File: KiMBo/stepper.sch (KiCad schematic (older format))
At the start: 22 parts

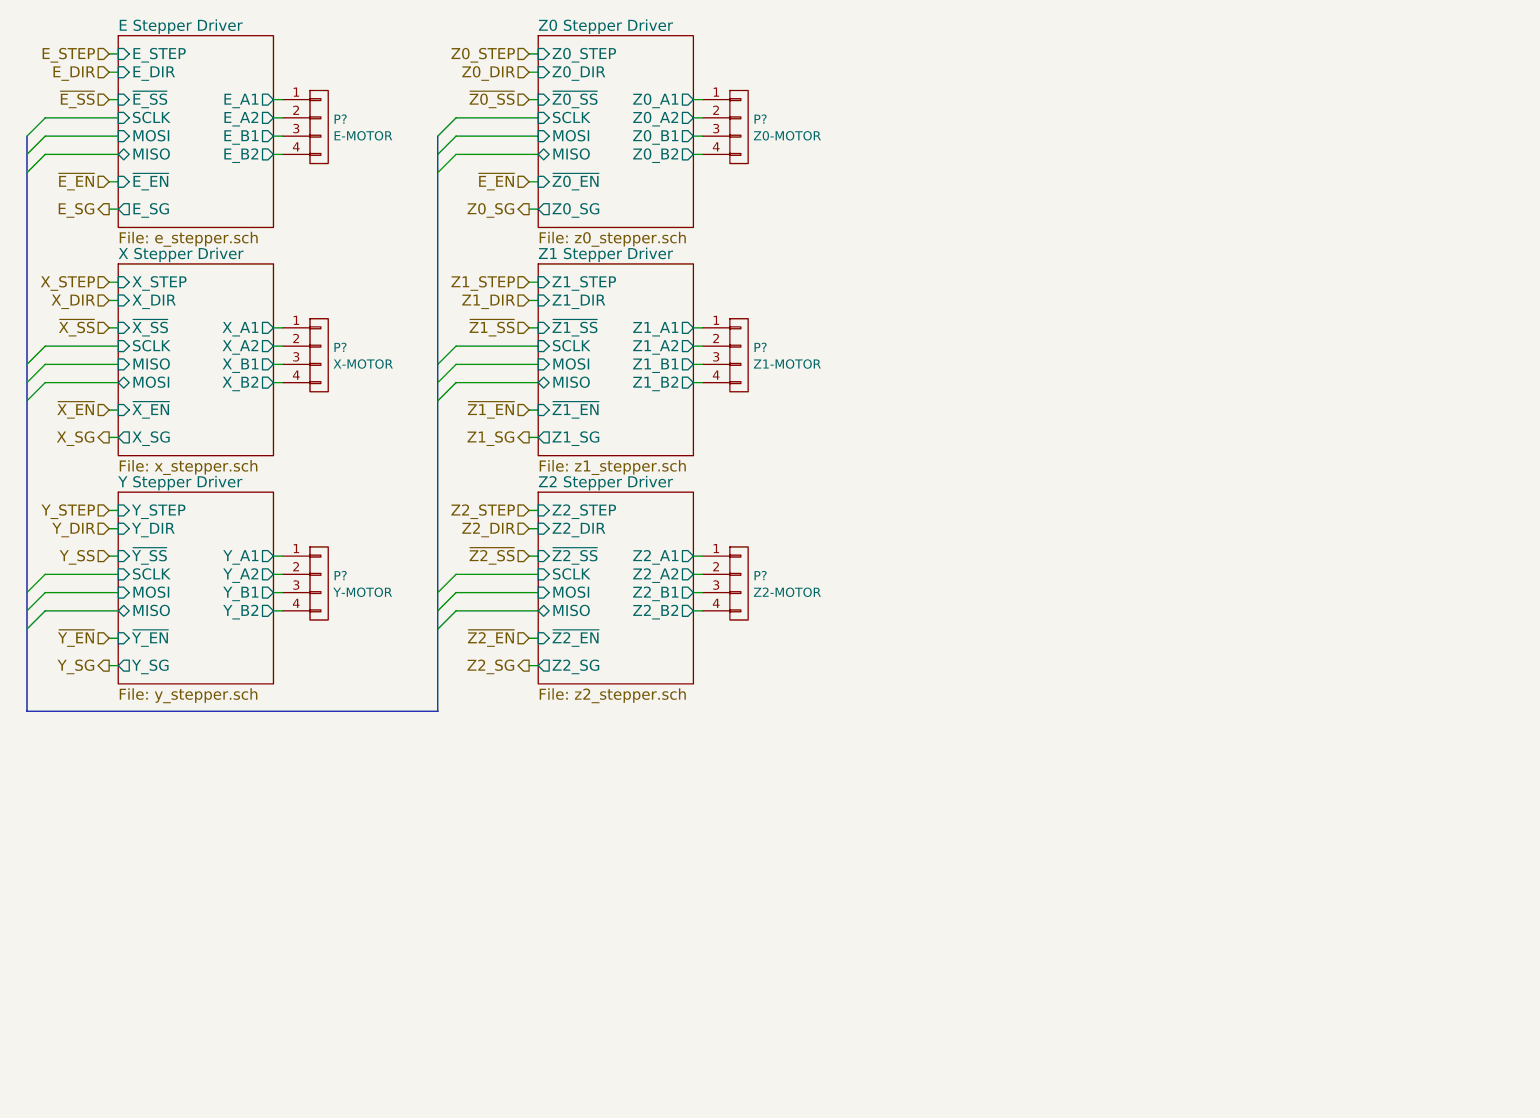
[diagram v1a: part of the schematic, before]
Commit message: Use the TMC2130 stepper driver, document and calculate the stepper motor current
The current to the motors are set by IRUN and IHOLD of the IHOLD_IRUN register
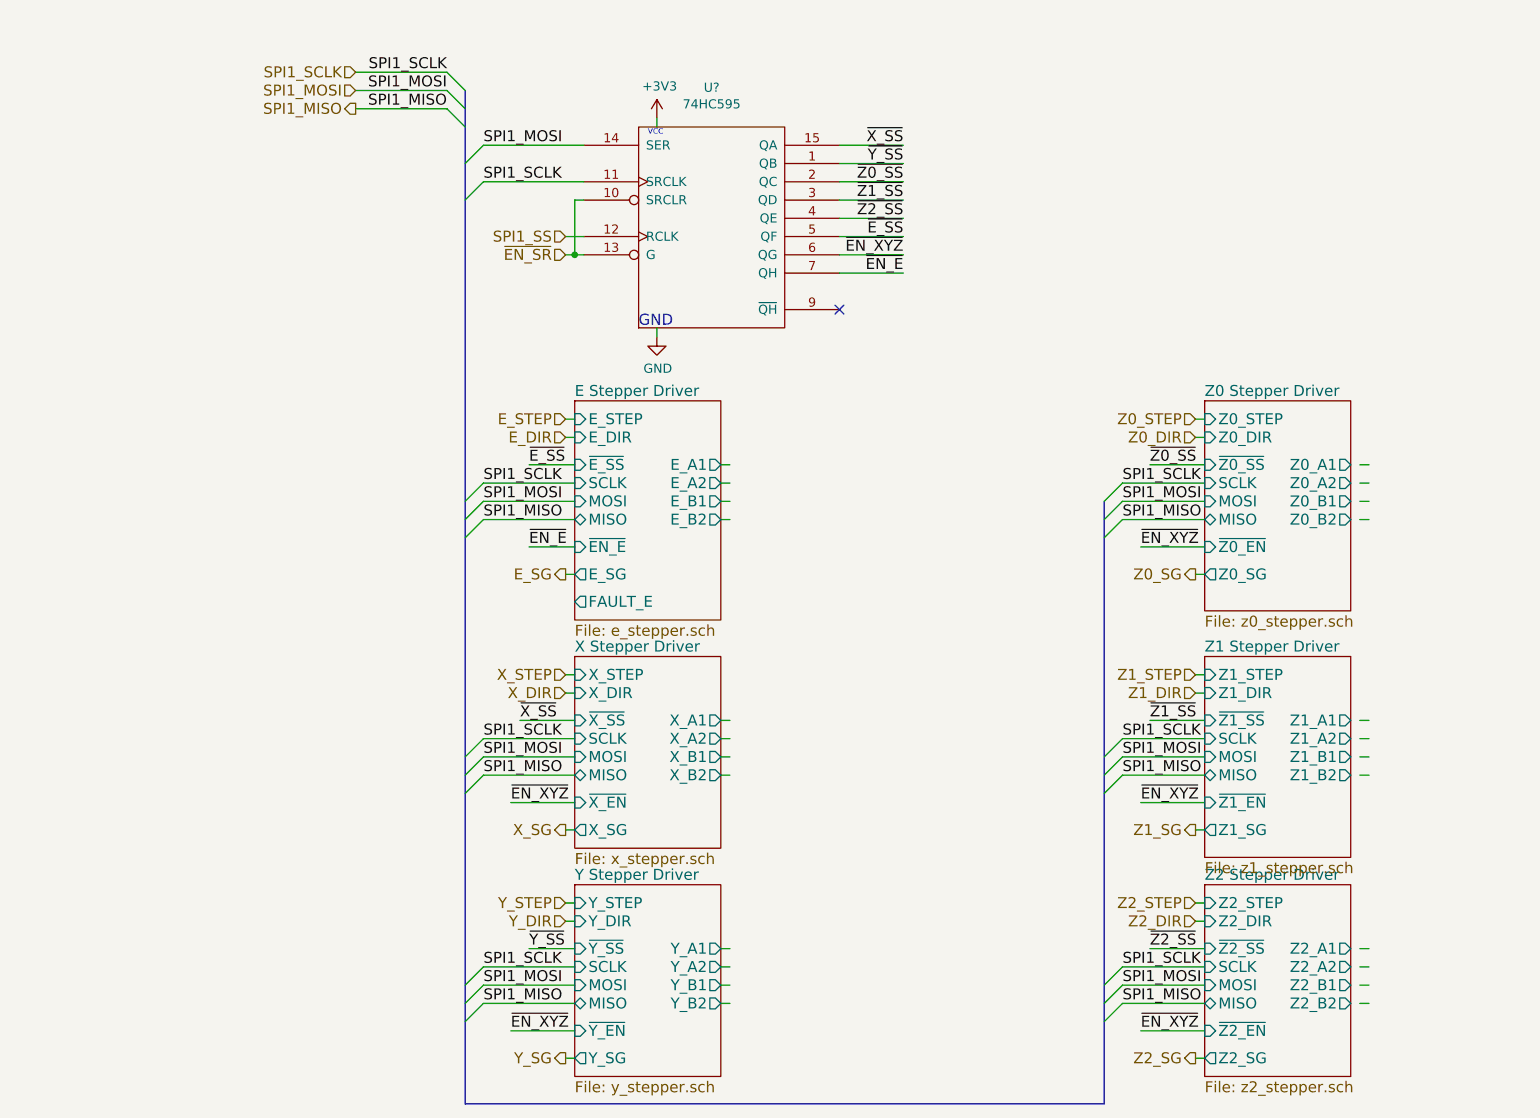
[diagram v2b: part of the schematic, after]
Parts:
- removed P?: E-MOTOR, symbol CONN_01X04
- removed P?: X-MOTOR, symbol CONN_01X04
- removed P?: Y-MOTOR, symbol CONN_01X04
- removed P?: Z0-MOTOR, symbol CONN_01X04
- removed P?: Z1-MOTOR, symbol CONN_01X04
- removed P?: Z2-MOTOR, symbol CONN_01X04
- added U?: 74HC595, symbol 74HC595
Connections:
- net labels added: +3V3, SPI1_MISO, SPI1_MOSI, SPI1_SCLK, SPI1_SS, ~EN_E, ~EN_SR, ~EN_XYZ, ~Y_SS
- net labels removed: Y_SS, ~E_EN, ~X_EN, ~Y_EN, ~Z1_EN, ~Z2_EN
- wire segments 124 -> 143
- no-connect marks 0 -> 1
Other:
- note added: "GND"
- note added: "VCC"

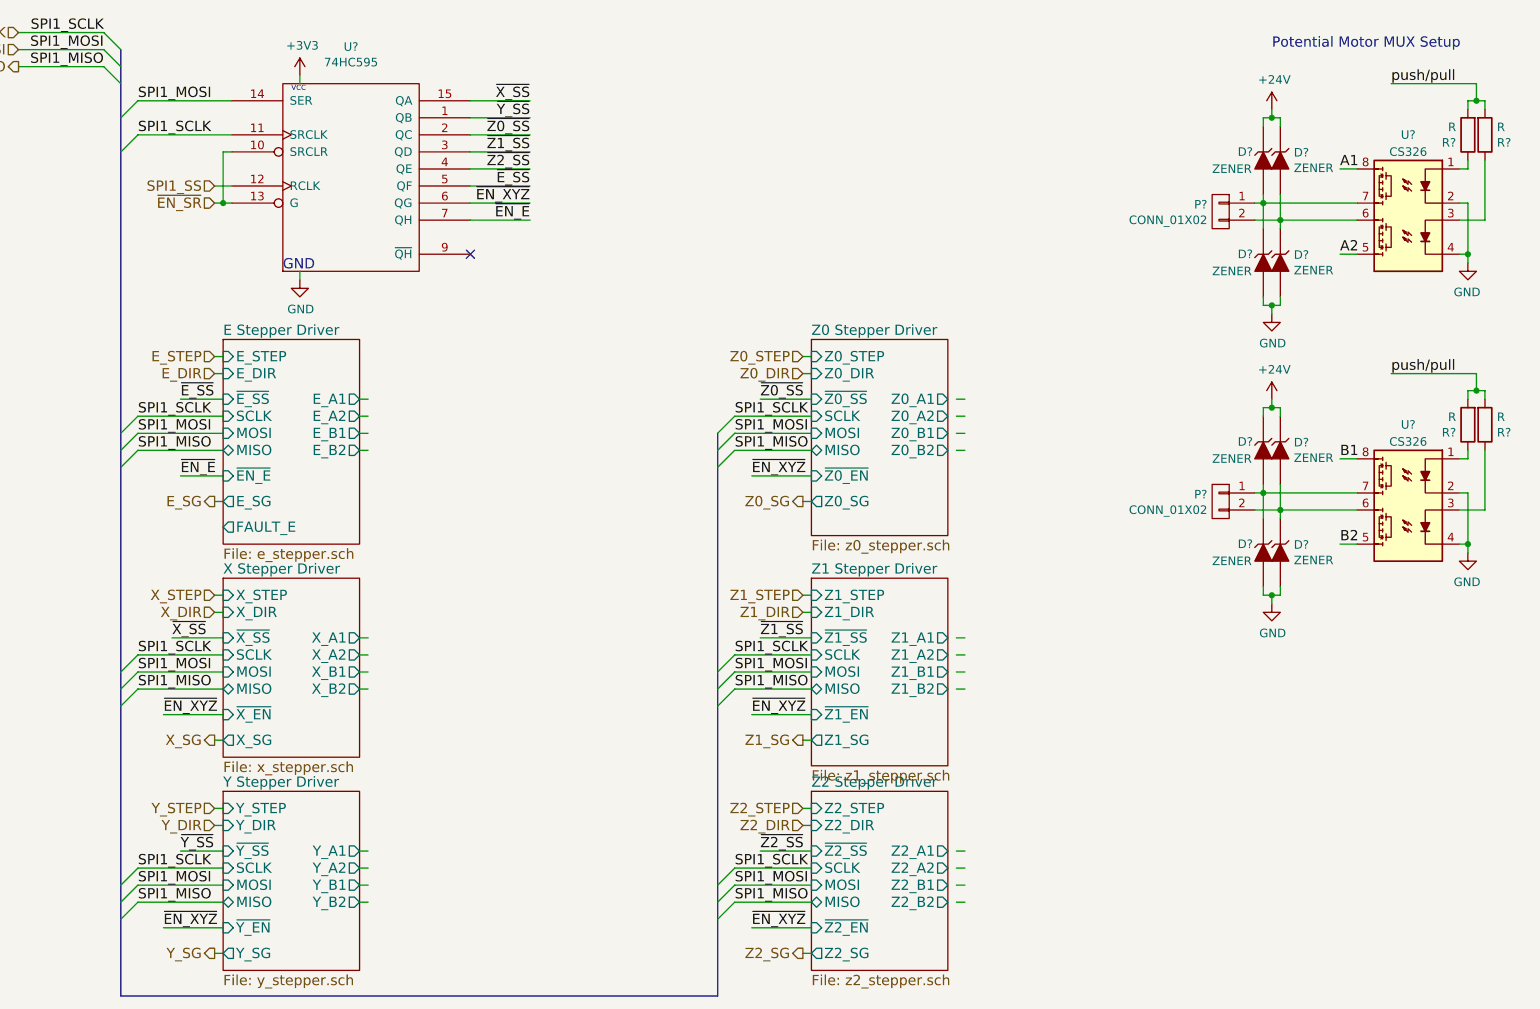
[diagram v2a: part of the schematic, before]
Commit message: Update the stepper schematics' passive components
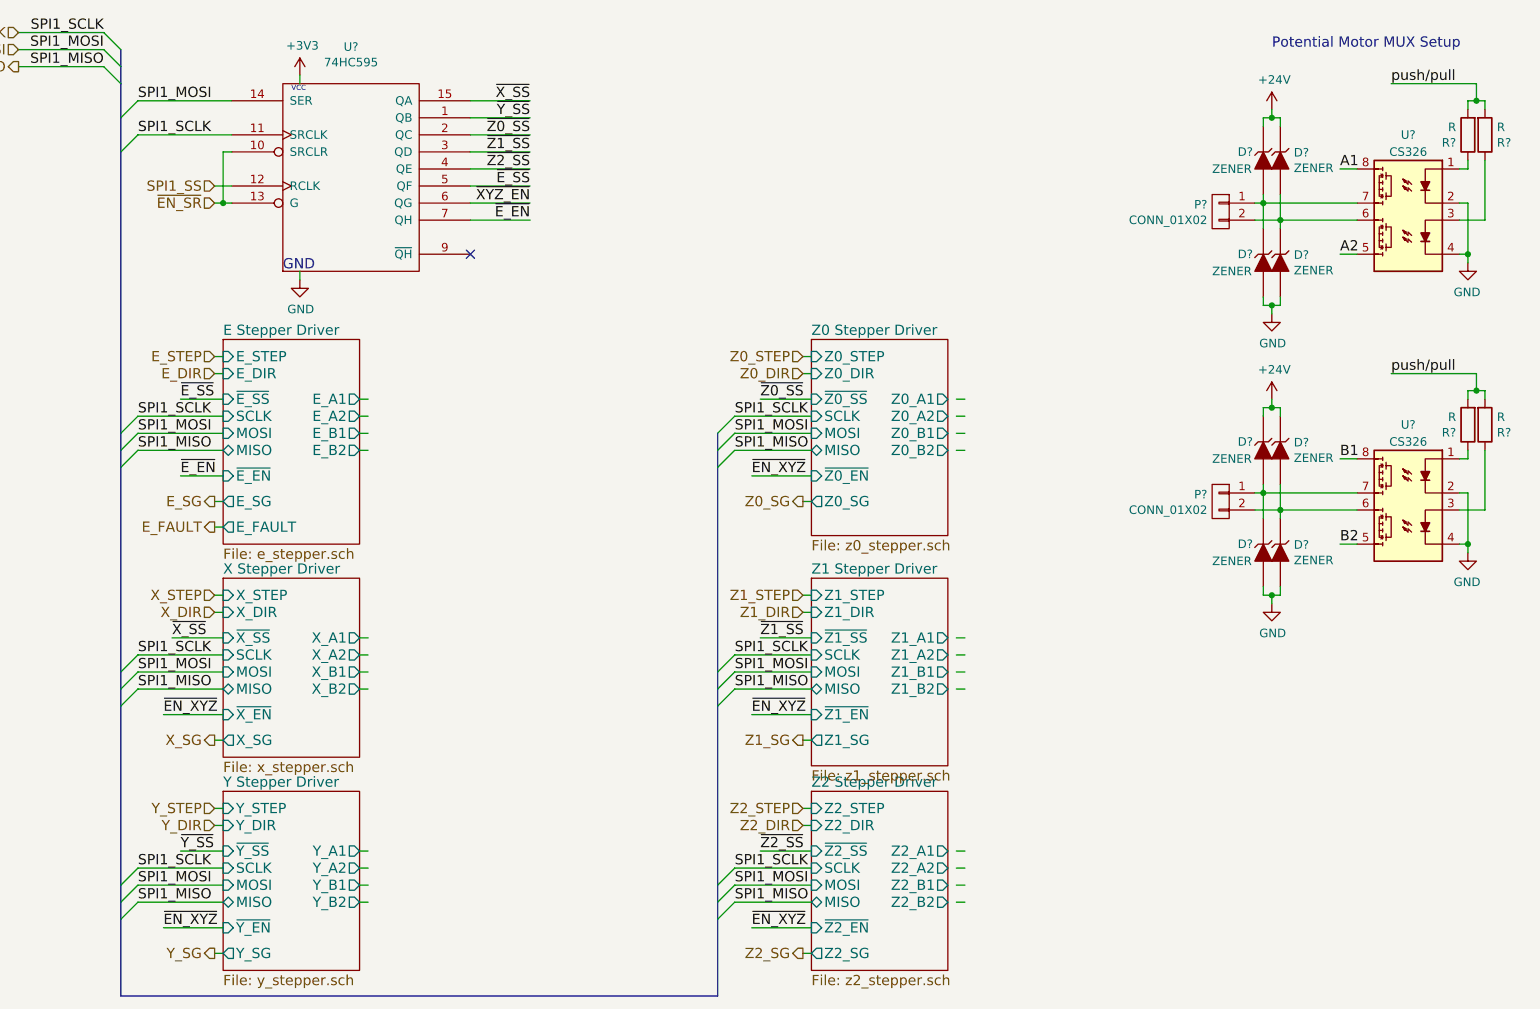
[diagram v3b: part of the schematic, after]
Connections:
- net labels added: E_FAULT, ~E_EN, ~XYZ_EN
- net labels removed: ~EN_E
- wire segments 143 -> 161
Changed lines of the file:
@@
 F10 "E_DIR" I L 5200 3100 60
 F11 "~E_SS" I L 5200 3250 60
-F12 "~EN_E" I L 5200 3700 60
+F12 "~E_EN" I L 5200 3700 60
 F13 "E_SG" O L 5200 3850 60
-F14 "FAULT_E" O L 5200 4000 60
+F14 "E_FAULT" O L 5200 4000 60
 $EndSheet
 $Sheet
@@
 ~Z2_SS
 Text Label 7000 2200 2    60   ~ 0
-~EN_E
+~E_EN
 Text Label 7000 2100 2    60   ~ 0
-~EN_XYZ
+~XYZ_EN
 NoConn ~ 6650 2400
 $Comp
@@
 ~Z2_SS
 Text Label 4950 3700 0    60   ~ 0
-~EN_E
+~E_EN
 Text Label 4900 4650 0    60   ~ 0
 ~X_SS
@@
 	4700 1700 5250 1700
 Wire Wire Line
-	5150 2100 5250 2100
+	5150 2100 5200 2100
+Wire Wire Line
+	5200 2100 5250 2100
 Wire Wire Line
 	5250 2000 5150 2000
@@
 Connection ~ 11400 3900
 Wire Wire Line
-	11400 3750 11400 3950
+	11400 3750 11400 3900
+Wire Wire Line
+	11400 3900 11400 3950
 Connection ~ 11300 3800
 Wire Wire Line
-	11300 3750 11300 3950
+	11300 3750 11300 3800
+Wire Wire Line
+	11300 3800 11300 3950
 Connection ~ 11350 4400
 Wire Wire Line
 	11350 4450 11350 4400
 Wire Wire Line
-	11300 4400 11400 4400
+	11300 4400 11350 4400
+Wire Wire Line
+	11350 4400 11400 4400
 Wire Wire Line
 	11400 4400 11400 4350
@@
 	11350 3300 11350 3250
 Wire Wire Line
-	11300 3300 11400 3300
+	11300 3300 11350 3300
+Wire Wire Line
+	11350 3300 11400 3300
 Wire Wire Line
 	11400 3300 11400 3350
@@
 	11850 3600 11750 3600
 Wire Wire Line
-	11250 3800 11850 3800
-Wire Wire Line
-	11250 3900 11850 3900
+	11250 3800 11300 3800
+Wire Wire Line
+	11300 3800 11850 3800
+Wire Wire Line
+	11250 3900 11400 3900
+Wire Wire Line
+	11400 3900 11850 3900
 Wire Wire Line
 	12550 3100 12050 3100
@@
 Connection ~ 12550 3200
 Wire Wire Line
-	12500 3200 12600 3200
+	12500 3200 12550 3200
+Wire Wire Line
+	12550 3200 12600 3200
 Wire Wire Line
 	12600 3200 12600 3250
@@
 	12500 3200 12500 3250
 Wire Wire Line
-	12500 3800 12500 4150
+	12500 3800 12500 4100
+Wire Wire Line
+	12500 4100 12500 4150
 Wire Wire Line
 	12450 4100 12500 4100
@@
 Connection ~ 11400 2200
 Wire Wire Line
-	11400 2050 11400 2250
+	11400 2050 11400 2200
+Wire Wire Line
+	11400 2200 11400 2250
 Connection ~ 11300 2100
 Wire Wire Line
-	11300 2050 11300 2250
+	11300 2050 11300 2100
+Wire Wire Line
+	11300 2100 11300 2250
 Connection ~ 11350 2700
 Wire Wire Line
 	11350 2750 11350 2700
 Wire Wire Line
-	11300 2700 11400 2700
+	11300 2700 11350 2700
+Wire Wire Line
+	11350 2700 11400 2700
 Wire Wire Line
 	11400 2700 11400 2650
@@
 	11350 1600 11350 1550
 Wire Wire Line
-	11300 1600 11400 1600
+	11300 1600 11350 1600
+Wire Wire Line
+	11350 1600 11400 1600
 Wire Wire Line
 	11400 1600 11400 1650
@@
 	11850 1900 11750 1900
 Wire Wire Line
-	11250 2100 11850 2100
-Wire Wire Line
-	11250 2200 11850 2200
+	11250 2100 11300 2100
+Wire Wire Line
+	11300 2100 11850 2100
+Wire Wire Line
+	11250 2200 11400 2200
+Wire Wire Line
+	11400 2200 11850 2200
 Wire Wire Line
 	12550 1400 12050 1400
@@
 Connection ~ 12550 1500
 Wire Wire Line
-	12500 1500 12600 1500
+	12500 1500 12550 1500
+Wire Wire Line
+	12550 1500 12600 1500
 Wire Wire Line
 	12600 1500 12600 1550
@@
 	12500 1500 12500 1550
 Wire Wire Line
-	12500 2100 12500 2450
+	12500 2100 12500 2400
+Wire Wire Line
+	12500 2400 12500 2450
 Wire Wire Line
 	12450 2400 12500 2400
@@
 	9500 3250 9550 3250
 Wire Bus Line
-	4600 1200 4600 6750
+	4600 1200 4600 1300
+Wire Bus Line
+	4600 1300 4600 1400
+Wire Bus Line
+	4600 1400 4600 1600
+Wire Bus Line
+	4600 1600 4600 1800
+Wire Bus Line
+	4600 1800 4600 3450
+Wire Bus Line
+	4600 3450 4600 3550
+Wire Bus Line
+	4600 3550 4600 3650
+Wire Bus Line
+	4600 3650 4600 4850
+Wire Bus Line
+	4600 4850 4600 4950
+Wire Bus Line
+	4600 4950 4600 5050
+Wire Bus Line
+	4600 5050 4600 6100
+Wire Bus Line
+	4600 6100 4600 6200
+Wire Bus Line
+	4600 6200 4600 6300
+Wire Bus Line
+	4600 6300 4600 6750
 Wire Wire Line
 	4700 3550 5200 3550
@@
 	4700 3350 5200 3350
 Wire Bus Line
-	8100 3450 8100 6750
+	8100 3450 8100 3550
+Wire Bus Line
+	8100 3550 8100 3650
+Wire Bus Line
+	8100 3650 8100 4850
+Wire Bus Line
+	8100 4850 8100 4950
+Wire Bus Line
+	8100 4950 8100 5050
+Wire Bus Line
+	8100 5050 8100 6100
+Wire Bus Line
+	8100 6100 8100 6200
+Wire Bus Line
+	8100 6200 8100 6300
+Wire Bus Line
+	8100 6300 8100 6750
 Wire Bus Line
 	8100 6750 4600 6750
@@
 Wire Wire Line
 	6000 6200 6050 6200
+Text HLabel 5150 4000 0    60   Output ~ 0
+E_FAULT
+Wire Wire Line
+	5200 4000 5150 4000
 $EndSCHEMATC
